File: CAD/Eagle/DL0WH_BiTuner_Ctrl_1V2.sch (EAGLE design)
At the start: 141 parts, among them Q0321 ABS07-32.768KHZ, U0101 STM32L476RXT_64PIN_LDO, U0601 MC33996, U0701 MC33996, U0801 MC33996, U0921 TS5A23166, U0951 OPA354, U1001 MAX232_SOIC16, U1101 MAX232_SOIC16, U1201 LM53603-Q1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

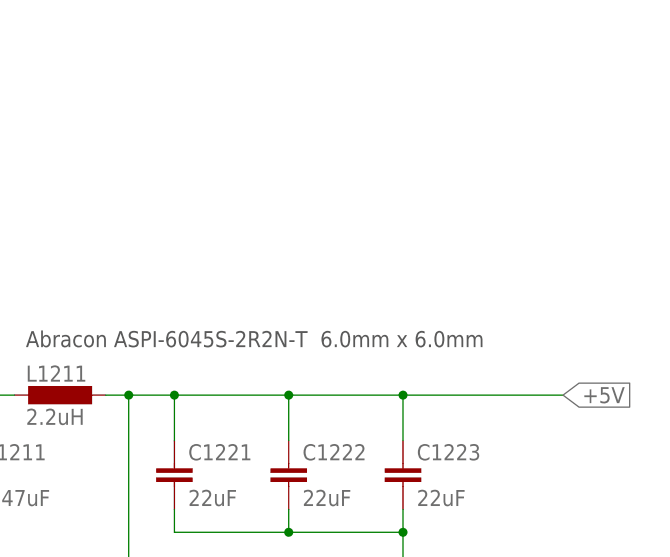
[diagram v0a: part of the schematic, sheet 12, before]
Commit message: HW_1V2 - CAD/Eagle - add CRS08 to power the 5V rail when no 12V is attached
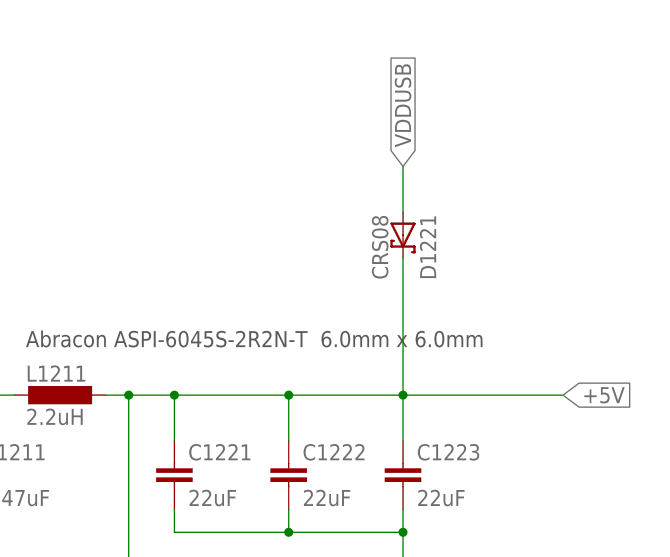
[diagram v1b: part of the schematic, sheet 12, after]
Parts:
- added D1221: CRS08, df4iah_diode:CRS08
- C0311: value 18pF -> 22pF
- C0332: value 8.2pF -> 18pF
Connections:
- net +5V: now also D1221.C
- net VDDUSB: now also D1221.A
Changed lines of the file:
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@@
 <part name="FRAME_03" library="df4iah_frame" deviceset="A4L-LOC" device="" value="I2C connector"/>
 <part name="Q0321" library="df4iah_crystal" deviceset="ABS07-32.768KHZ" device=""/>
-<part name="C0311" library="df4iah_rcl" deviceset="C-EU" device="C0402" value="18pF"/>
+<part name="C0311" library="df4iah_rcl" deviceset="C-EU" device="C0402" value="22pF"/>
 <part name="GND0311" library="df4iah_supply" deviceset="GND" device=""/>
 <part name="GND0331" library="df4iah_supply" deviceset="GND" device=""/>
@@
 <part name="R0231" library="df4iah_rcl" deviceset="R-EU_" device="R0402" value="220kR"/>
 <part name="R0232" library="df4iah_rcl" deviceset="R-EU_" device="R0402" value="220kR"/>
-<part name="C0332" library="df4iah_rcl" deviceset="C-EU" device="C0402" value="8.2pF"/>
+<part name="C0332" library="df4iah_rcl" deviceset="C-EU" device="C0402" value="18pF"/>
 <part name="GND0332" library="df4iah_supply" deviceset="GND" device=""/>
 <part name="R0511" library="df4iah_rcl" deviceset="R-EU_" device="R0402" value="1kR"/>
@@
 <part name="GND0006" library="df4iah_supply" deviceset="GND" device=""/>
 <part name="X0201" library="df4iah_connector" deviceset="2X05_1MM27_SHROUDED_CORTEX_JTAG_SWD" device="&quot;" value="FTSH-105-01-F-D-K"/>
+<part name="D1221" library="df4iah_diode" deviceset="CRS08" device=""/>
 </parts>
 <sheets>
@@
 <instance part="C1223" gate="G$1" x="208.28" y="116.84"/>
 <instance part="X1211" gate="G$1" x="12.7" y="106.68" rot="R180"/>
+<instance part="D1221" gate="G$1" x="208.28" y="142.24" rot="R270"/>
 </instances>
 <busses>
@@
 <wire x1="208.28" y1="124.46" x2="208.28" y2="119.38" width="0.1524" layer="91"/>
 <junction x="208.28" y="124.46"/>
+<pinref part="D1221" gate="G$1" pin="C"/>
+<wire x1="208.28" y1="124.46" x2="208.28" y2="139.7" width="0.1524" layer="91"/>
 </segment>
 </net>
@@
 </segment>
 </net>
+<net name="VDDUSB" class="0">
+<segment>
+<pinref part="D1221" gate="G$1" pin="A"/>
+<wire x1="208.28" y1="144.78" x2="208.28" y2="149.86" width="0.1524" layer="91"/>
+<label x="208.28" y="149.86" size="1.778" layer="95" rot="R90" xref="yes"/>
+</segment>
+</net>

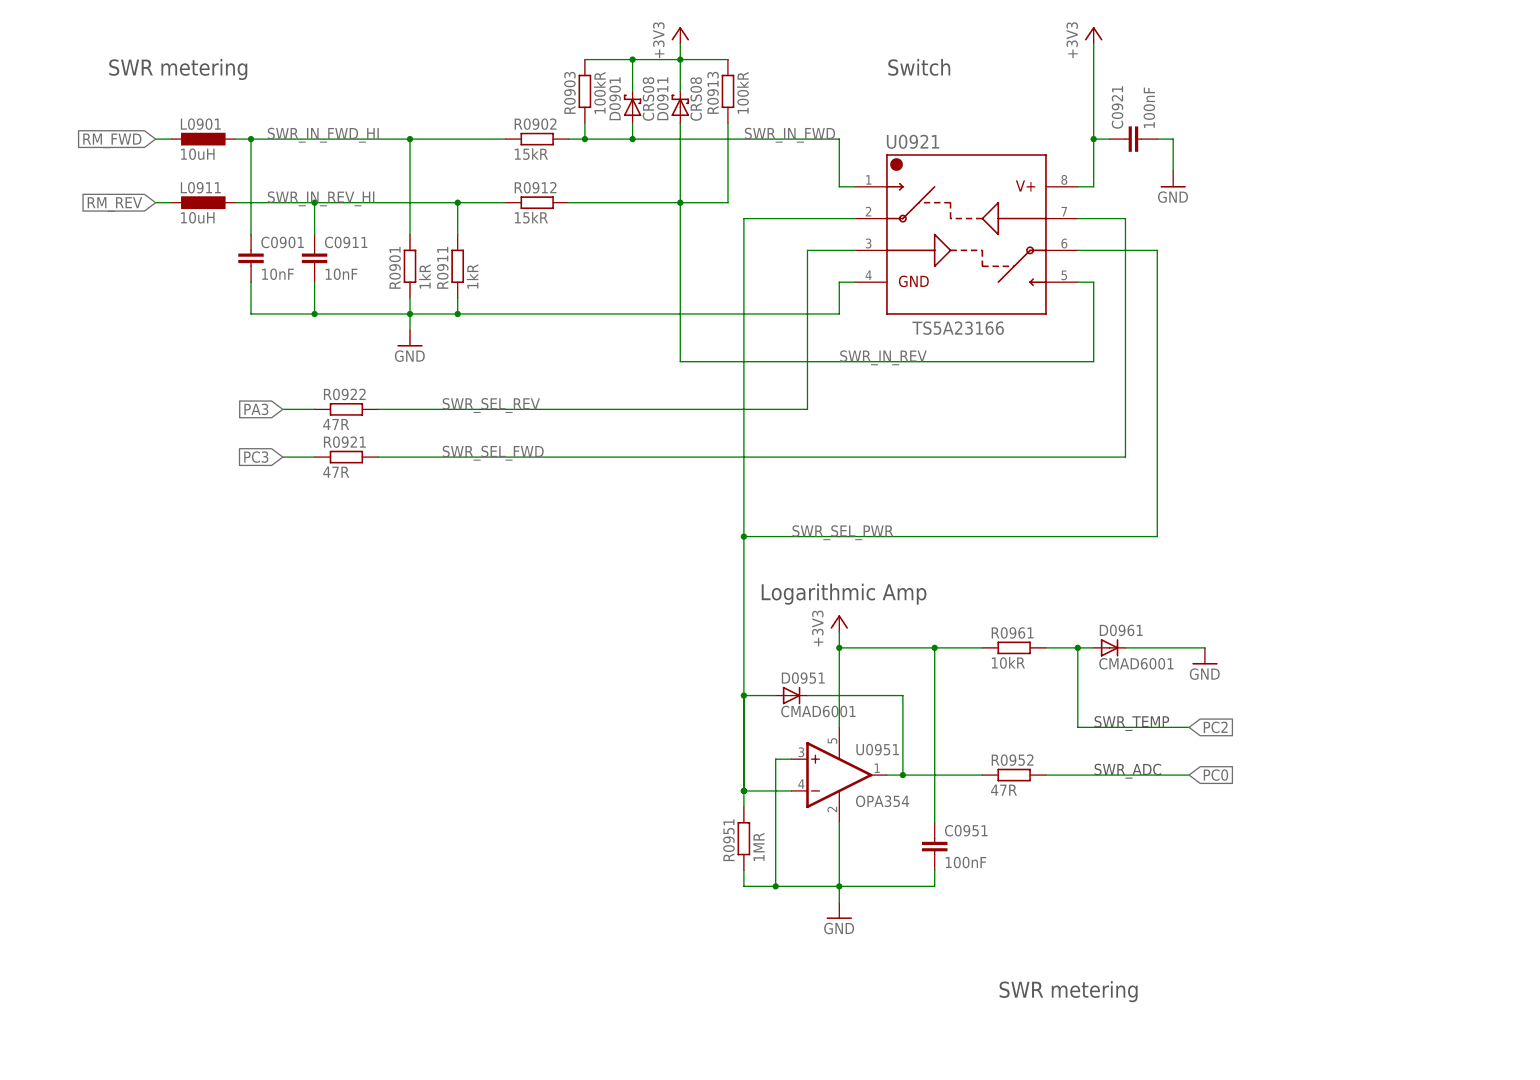
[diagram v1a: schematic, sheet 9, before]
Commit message: HW_1V2 - CAD/Eagle - LogAmp added
Signed-off-by: Ulrich Habel <espero7757@gmx.net>
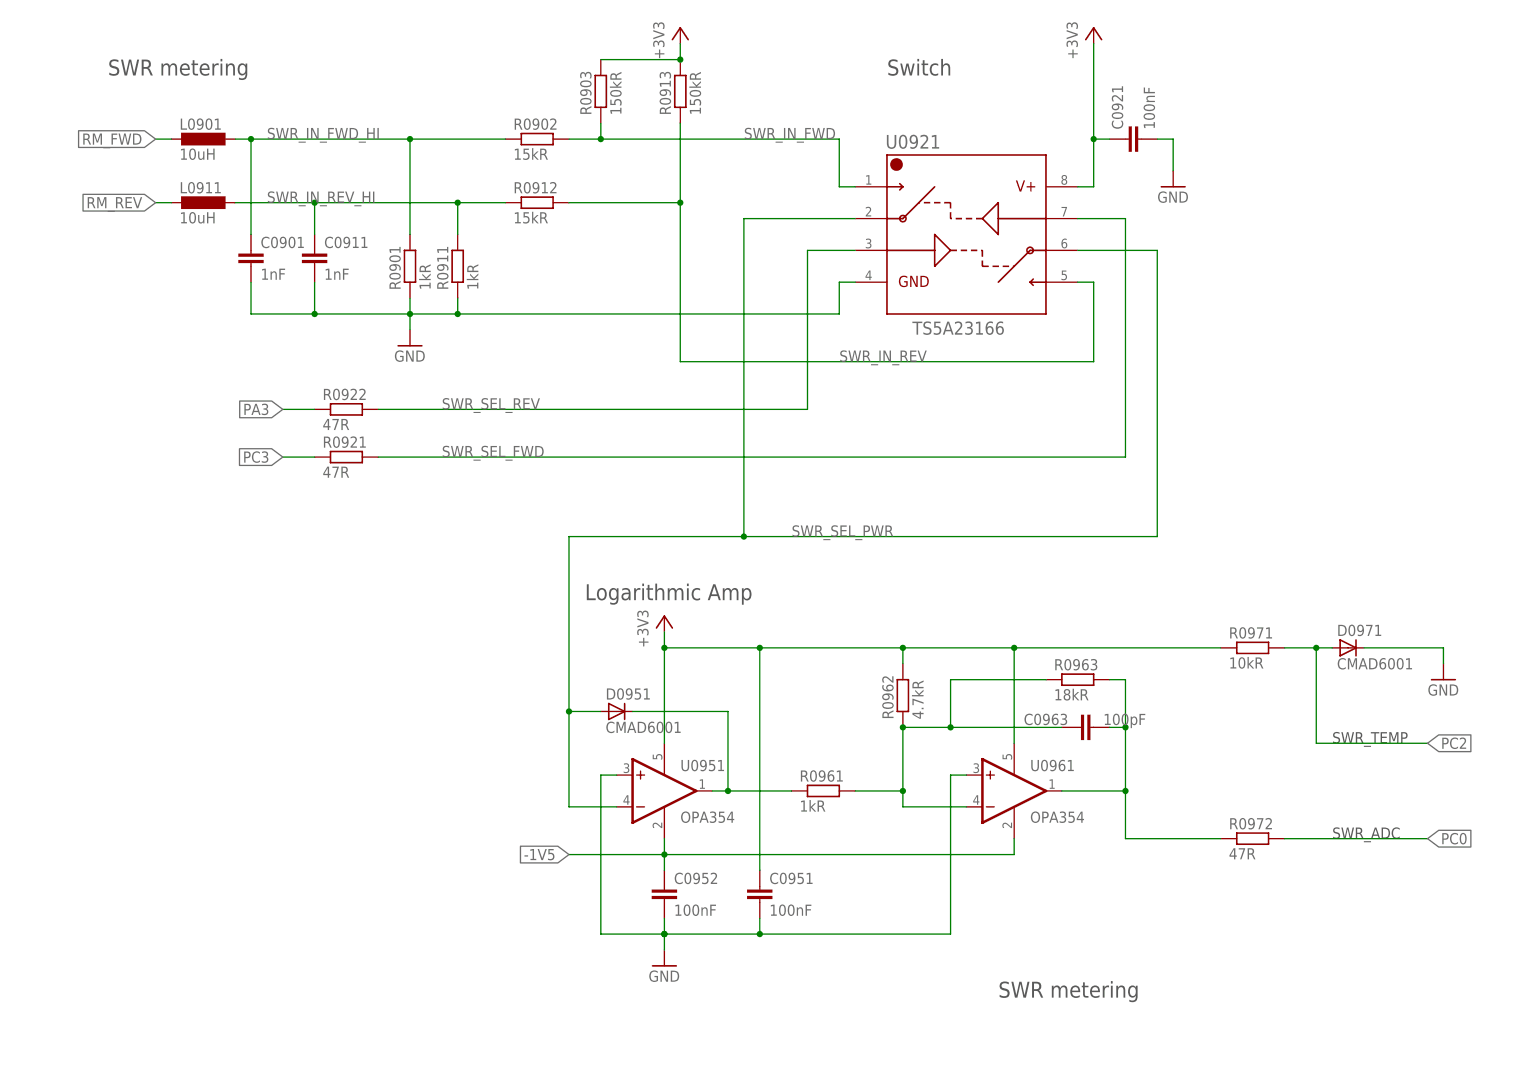
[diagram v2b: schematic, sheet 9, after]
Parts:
- removed D0901, D0911: CRS08, df4iah_diode:CRS08
- removed D0961: CMAD6001, df4iah_diode:D_SOD923
- removed R0951: 1MR, df4iah_rcl:R-EU_R0402
- removed R0952: 47R, df4iah_rcl:R-EU_R0402
- added C0952: 100nF, df4iah_rcl:C-EUC0402
- added C0963: 100pF, df4iah_rcl:C-EUC0402
- added D0971: CMAD6001, df4iah_diode:D_SOD923
- added R0962: 4.7kR, df4iah_rcl:R-EU_R0402
- added R0963: 18kR, df4iah_rcl:R-EU_R0402
- added R0971: 10kR, df4iah_rcl:R-EU_R0402
- added R0972: 47R, df4iah_rcl:R-EU_R0402
- added U0961: OPA354, df4iah_opamp:OPA354
- C0901, C0911: value 10nF -> 1nF
- R0903, R0913: value 100kR -> 150kR
- R0961: value 10kR -> 1kR
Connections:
- removed net SWR_OP_OUT: D0951.C, R0952.1, U0951.OUT
- new net -1V5: C0952.1, U0951.V-, U0961.V-
- new net SWR_OP1_OUT: D0951.C, R0961.1, U0951.OUT
- new net SWR_OP2_IN: C0963.1, R0961.2, R0962.1, R0963.1, U0961.-IN
- new net SWR_OP2_OUT: C0963.2, R0963.2, R0972.1, U0961.OUT
- net +3V3: now also R0962.2, R0971.1, U0961.V+; no longer D0901.C, D0911.C, R0961.1
- net GND: now also C0952.2, D0971.C, U0961.+IN; no longer D0961.C, R0951.1, U0951.V-
- net PC0: now also R0972.2; no longer R0952.2
- net PC2: now also D0971.A, R0971.2; no longer D0961.A, R0961.2
- net SWR_IN_FWD: no longer D0901.A
- net SWR_IN_REV: no longer D0911.A
- net SWR_SEL_PWR: no longer R0951.2
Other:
- moved on the sheet: C0951, D0951, R0903, R0913, R0961, U0951

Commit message: HW_1V2 - CAD/Eagle - LogAmp enhanced
Signed-off-by: Ulrich Habel <espero7757@gmx.net>
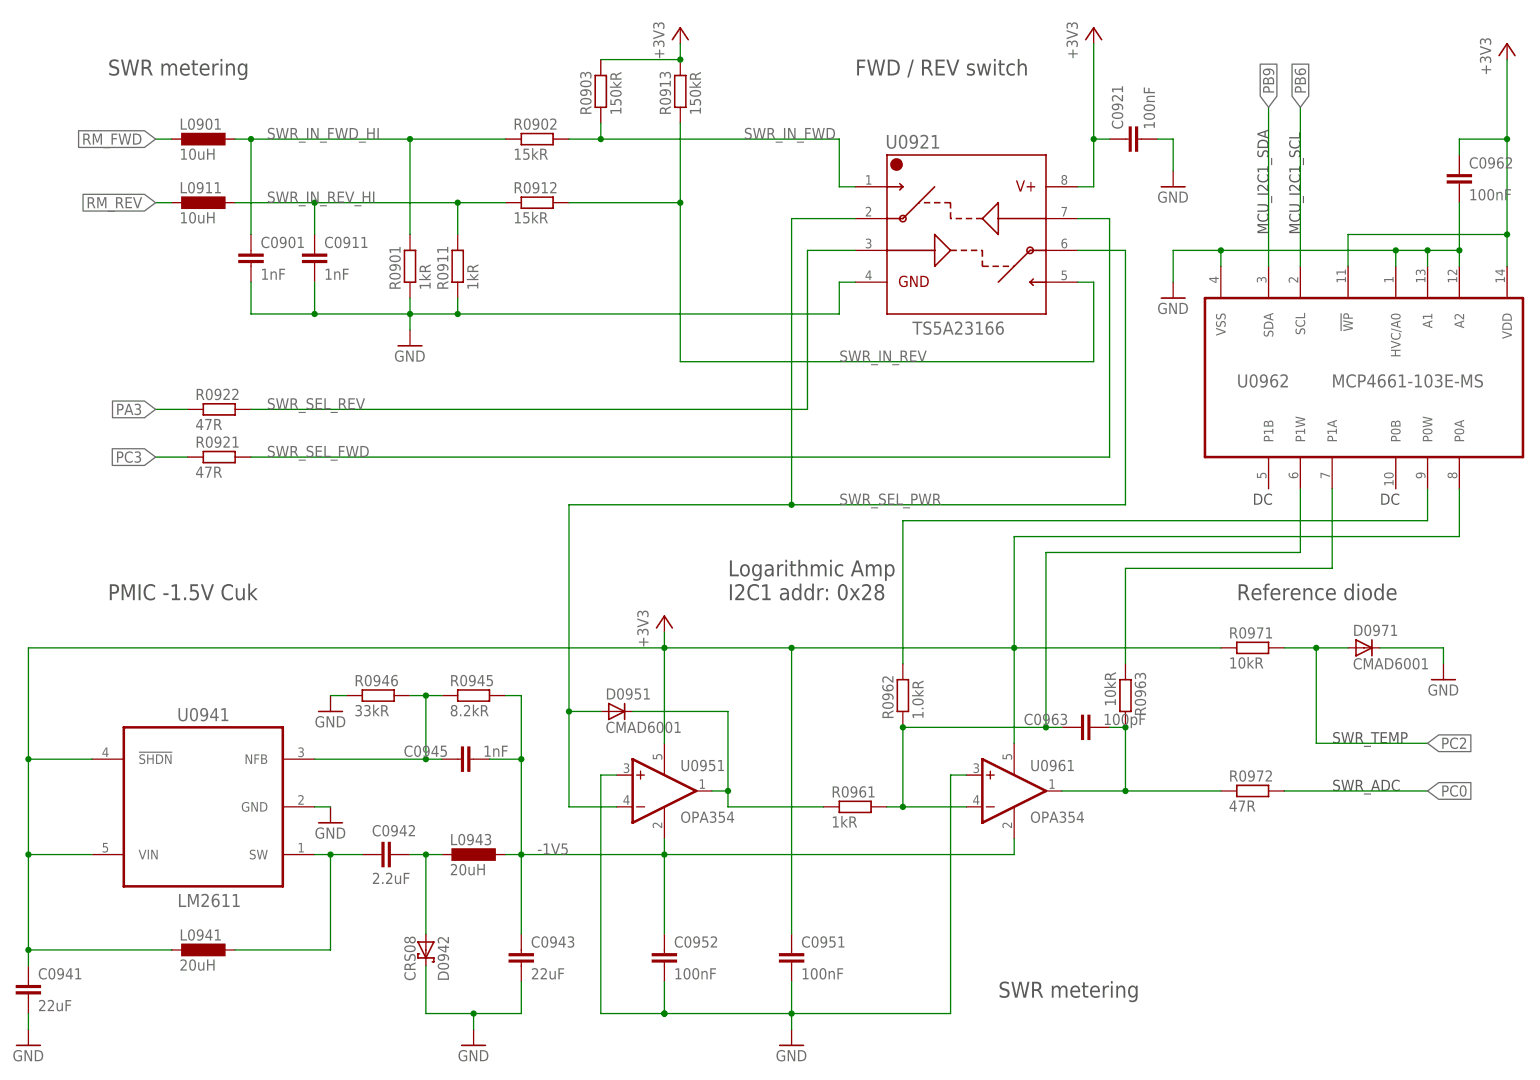
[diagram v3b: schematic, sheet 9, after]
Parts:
- added C0941, C0943: 22uF, df4iah_rcl:C-EUC0603
- added C0942: 2.2uF, df4iah_rcl:C-EUC0805
- added C0945: 1nF, df4iah_rcl:C-EUC0402
- added C0962: 100nF, df4iah_rcl:C-EUC0402
- added D0942: CRS08, df4iah_diode:CRS08
- added L0941, L0943: 20uH, df4iah_rcl:L-EUL1812
- added R0945: 8.2kR, df4iah_rcl:R-EU_R0402
- added R0946: 33kR, df4iah_rcl:R-EU_R0402
- added U0941: LM2611, df4iah_powersupply:LM2611
- added U0962: MCP4661-103E-MS, df4iah_dig-pot:MCP4661-104E-MS
- R0962: value 4.7kR -> 1.0kR
- R0963: value 18kR -> 10kR
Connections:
- new net LM2611_NFB: C0945.1, R0945.1, R0946.2, U0941.NFB
- new net LM2611_SW: C0942.1, L0941.1, U0941.SW
- new net LM_DA: C0942.2, D0942.A, L0943.2
- new net OPA_FB: R0963.1, U0962.P1A
- new net OPA_PULL: R0962.2, U0962.P0W
- net +3V3: now also C0941.1, C0962.1, L0941.2, U0941.!SHDN, U0941.VIN, U0962.!WP, U0962.P0A, U0962.VDD; no longer R0962.2
- net -1V5: now also C0943.1, C0945.2, L0943.1, R0945.2
- net GND: now also C0941.2, C0943.2, C0962.2, D0942.C, R0946.1, U0941.GND, U0962.A1, U0962.A2, U0962.HVC/A0, U0962.VSS
- net PB6: now also U0962.SCL
- net PB9: now also U0962.SDA
- net SWR_OP2_IN: now also U0962.P1W; no longer R0963.1
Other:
- note added: "Addr Device 0x28 PMIC 1.2V voltage regulation"
- note added: "DC"
- note added: "FWD / REV switch"
- note added: "Logarithmic Amp I2C1 addr: 0x28"
- note added: "PMIC -1.5V Cuk"
- note added: "Reference diode"
- note removed: "Addr Device"
- note removed: "Logarithmic Amp"
- note removed: "Switch"
- moved on the sheet: C0951, C0952, D0971, R0921, R0922, R0961, R0963, R0972

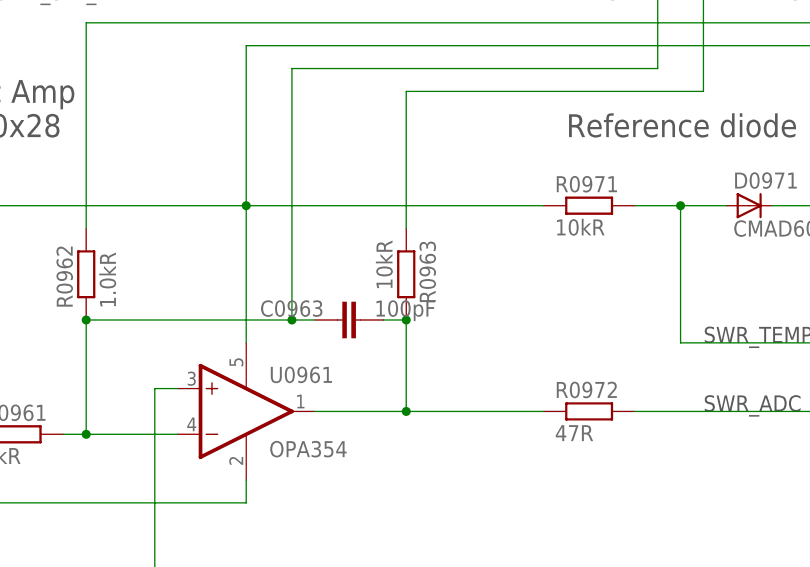
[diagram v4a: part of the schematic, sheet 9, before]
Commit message: HW_1V2 - CAD/Eagle - new LogAmp module placed
Signed-off-by: Ulrich Habel <espero7757@gmx.net>
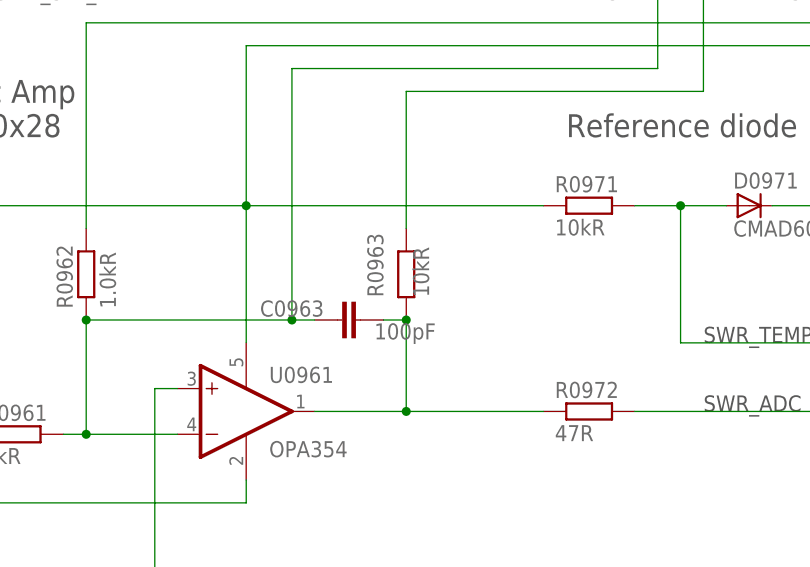
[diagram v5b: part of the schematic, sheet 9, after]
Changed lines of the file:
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@@
 <instance part="R0961" gate="G$1" x="142.24" y="45.72"/>
 <instance part="R0962" gate="G$1" x="149.86" y="63.5" rot="R90"/>
-<instance part="R0963" gate="G$1" x="185.42" y="63.5" rot="R270"/>
+<instance part="R0963" gate="G$1" x="185.42" y="63.5" smashed="yes" rot="R270">
+<attribute name="NAME" x="182.88" y="60.96" size="1.778" layer="95" rot="R90"/>
+<attribute name="VALUE" x="187.96" y="60.96" size="1.778" layer="96" rot="R90"/>
+</instance>
 <instance part="C0963" gate="G$1" x="177.8" y="58.42" smashed="yes" rot="R90">
 <attribute name="NAME" x="169.164" y="58.801" size="1.778" layer="95"/>
-<attribute name="VALUE" x="181.864" y="58.801" size="1.778" layer="96"/>
+<attribute name="VALUE" x="181.864" y="56.261" size="1.778" layer="96"/>
 </instance>
 <instance part="U0941" gate="G$1" x="38.1" y="45.72" smashed="yes" rot="R180">
